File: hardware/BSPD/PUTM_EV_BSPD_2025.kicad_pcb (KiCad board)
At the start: 4 copper layers, 63 x 37.5 mm, 85 parts, among them J1 BS1, J2 BS2, J3 BS2, J4 Conn_01x02, J5 SDC, K2 TE AXICOM IM07DTS, Q1 BS170F, U1 MC78M12CDTG, U10 LM393B, U12 74AHC1G08, U13 LM393B, U2 LM1117IMP-5.0, U3 74HC2G14-Q100, U4 LM393B, U5 74AHC1G08, U6 74HC2G14-Q100, U7 LM393B, U8 NE555DR, U9 74HC1G32GV

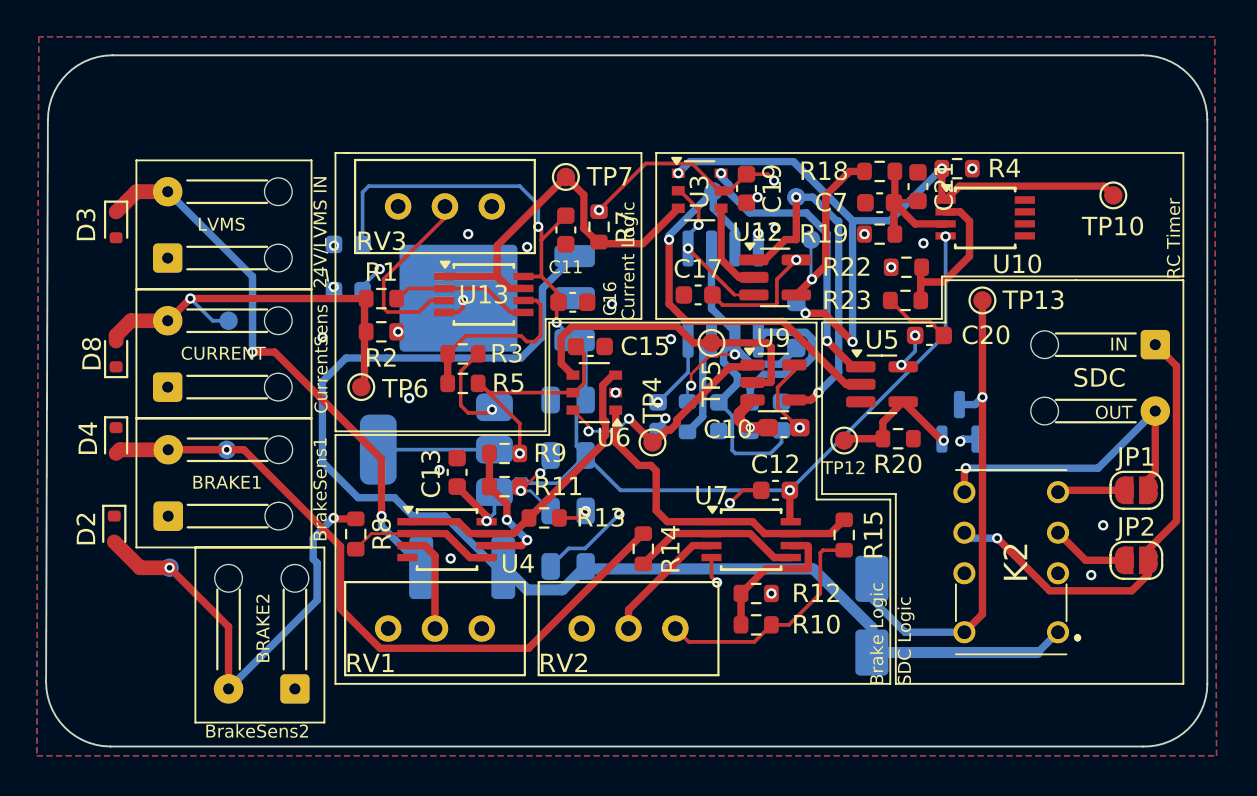
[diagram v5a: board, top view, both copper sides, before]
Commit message: Fixed mounting hole issues.
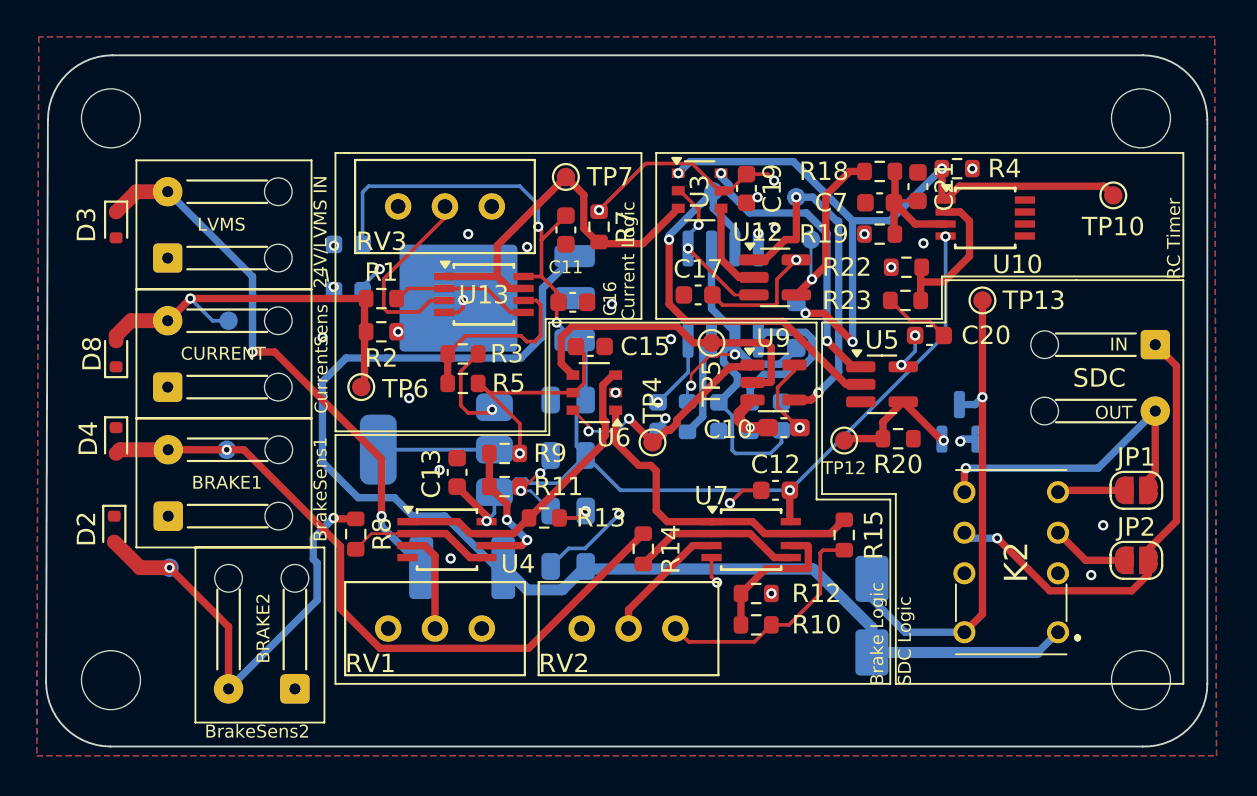
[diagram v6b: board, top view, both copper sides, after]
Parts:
- added H1: MountingHole, MountingHole:MountingHole_3.2mm_M3_ISO7380, F.Cu at (113.0, 87.4)
- added H2: MountingHole, MountingHole:MountingHole_3.2mm_M3_ISO7380, F.Cu at (113.0, 117.9)
- added H3: MountingHole, MountingHole:MountingHole_3.2mm_M3_ISO7380, F.Cu at (168.9, 87.4)
- added H4: MountingHole, MountingHole:MountingHole_3.2mm_M3_ISO7380, F.Cu at (168.9, 117.9)
